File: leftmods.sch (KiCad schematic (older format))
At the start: 0 parts

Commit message: Added left modifiers to schematic
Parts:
- added DLM1, DLM2, DLM3: 1N4148WS, symbol D
- added LA1, LA2, LA3, LC2, LW1, LW2: MX-1.5U, symbol MX-1.5U
- added LC1: MX-1.25U, symbol MX-1.25U
- added RLM1, RLM2, RLM?: 2.2k, symbol R
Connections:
- new net: DLM1.1 (K), LC1.1 (COL), LC2.1 (COL)
- new net: LC1.3 (LED), LC2.3 (LED), RLM1.1
- new net: DLM2.1 (K), LA1.1 (COL), LW1.1 (COL), LW2.1 (COL)
- new net: LA1.3 (LED), LW1.3 (LED), LW2.3 (LED), RLM2.1
- new net: DLM3.1 (K), LA2.1 (COL), LA3.1 (COL)
- new net: LA2.3 (LED), LA3.3 (LED), RLM?.1
- new net leftmods5V: RLM1.2, RLM2.2, RLM?.2
- new net leftmodsLEDGND: LA1.4 (LEDGND), LA2.4 (LEDGND), LA3.4 (LEDGND), LC1.4 (LEDGND), LC2.4 (LEDGND), LW1.4 (LEDGND), LW2.4 (LEDGND)
- new net leftmodscol1: DLM1.2 (A)
- new net leftmodscol2: DLM2.2 (A)
- new net leftmodscol3: DLM3.2 (A)
- new net leftmodsrow: LA1.2 (ROW), LA2.2 (ROW), LA3.2 (ROW), LC1.2 (ROW), LC2.2 (ROW), LW1.2 (ROW), LW2.2 (ROW)

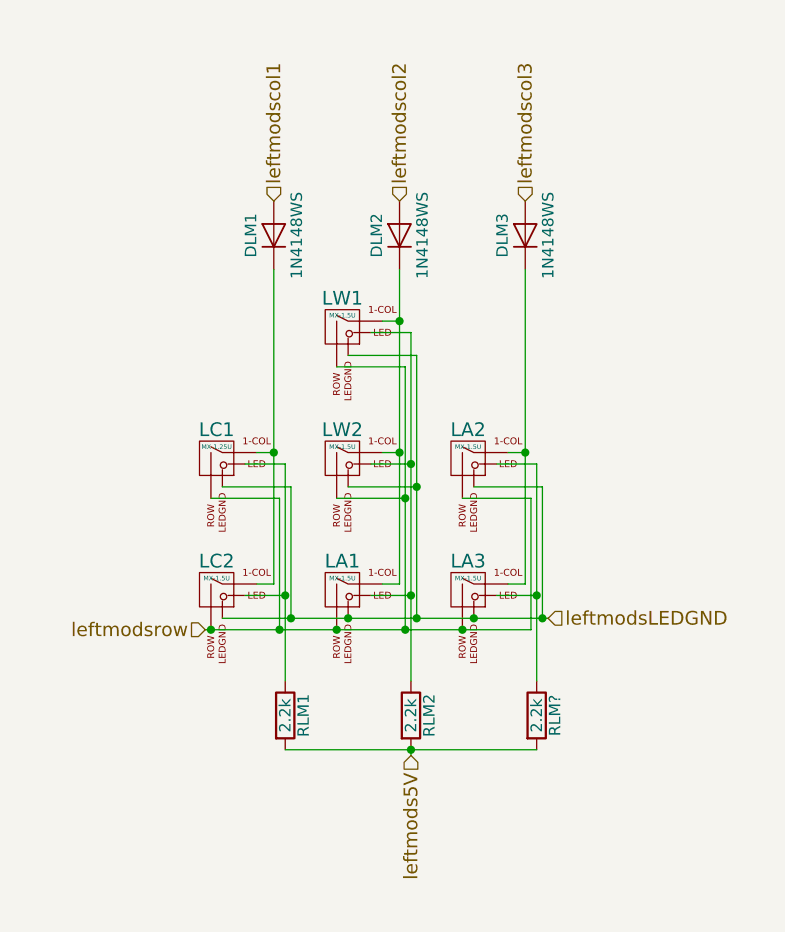
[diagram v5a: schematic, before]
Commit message: Added left mods to matrix
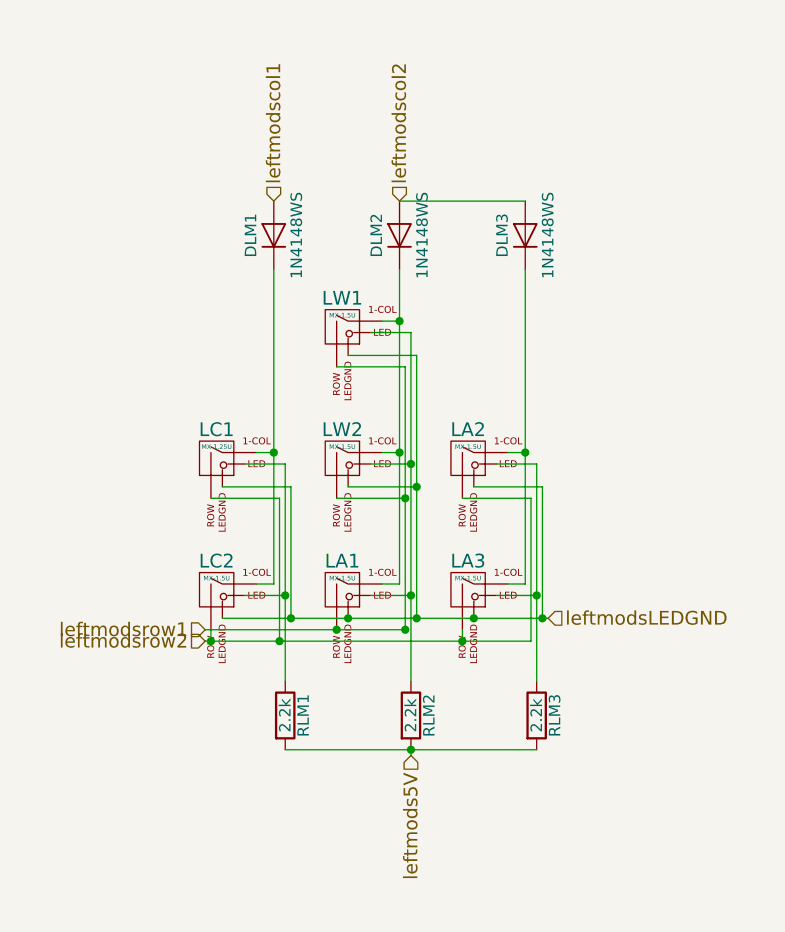
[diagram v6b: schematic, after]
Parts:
- gave numbers to parts that had none: 1
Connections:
- net leftmodscol3 is gone; now on net leftmodscol2: DLM3.2 (A)
- net leftmodsrow renamed leftmodsrow2
- net leftmodsrow2: no longer LA1.2 (ROW), LW1.2 (ROW), LW2.2 (ROW)
- new net leftmodsrow1: LA1.2 (ROW), LW1.2 (ROW), LW2.2 (ROW)
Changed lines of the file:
@@
 LIBS:valves
 LIBS:MX_Alps_Hybrids
-LIBS:Matrix-cache
+LIBS:ws2812b
+LIBS:Kairos-cache
 EELAYER 25 0
 EELAYER END
 $Descr A4 11693 8268
 encoding utf-8
-Sheet 1 6
+Sheet 6 7
 Title ""
 Date ""
@@
 $EndComp
 Text HLabel 4200 5450 0    60   Input ~ 0
-leftmodsrow
-Wire Wire Line
-	4975 4100 5050 4100
-Wire Wire Line
-	5050 3875 5050 5250
-Wire Wire Line
-	5050 4675 4975 4675
-Wire Wire Line
-	5050 5250 4975 5250
-Connection ~ 5050 4675
-Wire Wire Line
-	5525 4675 5600 4675
-Wire Wire Line
-	5600 3875 5600 5250
-Wire Wire Line
-	5600 5250 5525 5250
-Wire Wire Line
-	4425 4675 4500 4675
-Wire Wire Line
-	4500 3875 4500 5250
-Wire Wire Line
-	4500 5250 4425 5250
-Wire Wire Line
-	4775 4300 5075 4300
-Wire Wire Line
-	5075 4300 5075 5450
-Wire Wire Line
-	5075 4875 4775 4875
-Wire Wire Line
-	4200 5450 5625 5450
-Connection ~ 5075 4875
-Wire Wire Line
-	4225 4875 4525 4875
-Wire Wire Line
-	4525 4875 4525 5450
-Connection ~ 4775 5450
-Connection ~ 4525 5450
-Wire Wire Line
-	5325 4875 5625 4875
-Wire Wire Line
-	5625 4875 5625 5450
-Connection ~ 5075 5450
-Connection ~ 5325 5450
-Wire Wire Line
-	4375 4725 4550 4725
-Wire Wire Line
-	4550 4725 4550 5675
-Wire Wire Line
-	4550 5300 4375 5300
-Wire Wire Line
-	4275 5400 5700 5400
-Wire Wire Line
-	4575 5400 4575 4825
-Wire Wire Line
-	4575 4825 4275 4825
-Connection ~ 4575 5400
-Wire Wire Line
-	4925 4725 5100 4725
-Wire Wire Line
-	5100 4150 5100 5675
-Wire Wire Line
-	5100 5300 4925 5300
-Wire Wire Line
-	4925 4150 5100 4150
-Connection ~ 5100 4725
-Wire Wire Line
-	4825 4825 5125 4825
-Wire Wire Line
-	5125 4250 5125 5400
-Connection ~ 4825 5400
-Wire Wire Line
-	4825 4250 5125 4250
-Connection ~ 5125 4825
-Wire Wire Line
-	5475 4725 5650 4725
-Wire Wire Line
-	5650 4725 5650 5675
-Wire Wire Line
-	5650 5300 5475 5300
-Connection ~ 5125 5400
-Wire Wire Line
-	5675 5400 5675 4825
-Wire Wire Line
-	5675 4825 5375 4825
-Connection ~ 5375 5400
-Connection ~ 4225 5450
+leftmodsrow1
 $Comp
 L D DLM1
@@
 	0    -1   -1   0
 $EndComp
-Connection ~ 4500 4675
 $Comp
 L D DLM2
@@
 	0    -1   -1   0
 $EndComp
-Connection ~ 5050 4100
 $Comp
 L D DLM3
@@
 	0    -1   -1   0
 $EndComp
-Connection ~ 5600 4675
 Text HLabel 4500 3575 1    60   Input ~ 0
 leftmodscol1
 Text HLabel 5050 3575 1    60   Input ~ 0
 leftmodscol2
-Text HLabel 5600 3575 1    60   Input ~ 0
-leftmodscol3
 $Comp
 L R RLM1
@@
 	1    0    0    -1
 $EndComp
-Connection ~ 4550 5300
 $Comp
 L R RLM2
@@
 	1    0    0    -1
 $EndComp
-Connection ~ 5100 5300
-$Comp
-L R RLM?
+$Comp
+L R RLM3
 U 1 1 591D444F
 P 5650 5825
-F 0 "RLM?" V 5730 5825 50  0000 C CNN
+F 0 "RLM3" V 5730 5825 50  0000 C CNN
 F 1 "2.2k" V 5650 5825 50  0000 C CNN
 F 2 "" V 5580 5825 50  0000 C CNN
@@
 	1    0    0    -1
 $EndComp
+Text HLabel 5700 5400 2    60   Input ~ 0
+leftmodsLEDGND
+Text HLabel 5100 6000 3    60   Input ~ 0
+leftmods5V
+Text HLabel 4200 5500 0    60   Input ~ 0
+leftmodsrow2
+Wire Wire Line
+	4975 4100 5050 4100
+Wire Wire Line
+	5050 3875 5050 5250
+Wire Wire Line
+	5050 4675 4975 4675
+Wire Wire Line
+	5050 5250 4975 5250
+Connection ~ 5050 4675
+Wire Wire Line
+	5525 4675 5600 4675
+Wire Wire Line
+	5600 3875 5600 5250
+Wire Wire Line
+	5600 5250 5525 5250
+Wire Wire Line
+	4425 4675 4500 4675
+Wire Wire Line
+	4500 3875 4500 5250
+Wire Wire Line
+	4500 5250 4425 5250
+Wire Wire Line
+	4775 4300 5075 4300
+Wire Wire Line
+	5075 4300 5075 5450
+Wire Wire Line
+	5075 4875 4775 4875
+Wire Wire Line
+	5075 5450 4200 5450
+Connection ~ 5075 4875
+Wire Wire Line
+	4225 4875 4525 4875
+Connection ~ 4775 5450
+Wire Wire Line
+	5325 4875 5625 4875
+Wire Wire Line
+	5625 4875 5625 5500
+Connection ~ 5075 5450
+Wire Wire Line
+	4375 4725 4550 4725
+Wire Wire Line
+	4550 4725 4550 5675
+Wire Wire Line
+	4550 5300 4375 5300
+Wire Wire Line
+	4275 5400 5700 5400
+Wire Wire Line
+	4575 5400 4575 4825
+Wire Wire Line
+	4575 4825 4275 4825
+Connection ~ 4575 5400
+Wire Wire Line
+	4925 4725 5100 4725
+Wire Wire Line
+	5100 4150 5100 5675
+Wire Wire Line
+	5100 5300 4925 5300
+Wire Wire Line
+	4925 4150 5100 4150
+Connection ~ 5100 4725
+Wire Wire Line
+	4825 4825 5125 4825
+Wire Wire Line
+	5125 4250 5125 5400
+Connection ~ 4825 5400
+Wire Wire Line
+	4825 4250 5125 4250
+Connection ~ 5125 4825
+Wire Wire Line
+	5475 4725 5650 4725
+Wire Wire Line
+	5650 4725 5650 5675
+Wire Wire Line
+	5650 5300 5475 5300
+Connection ~ 5125 5400
+Wire Wire Line
+	5675 5400 5675 4825
+Wire Wire Line
+	5675 4825 5375 4825
+Connection ~ 5375 5400
+Connection ~ 4500 4675
+Connection ~ 5050 4100
+Connection ~ 5600 4675
+Connection ~ 4550 5300
+Connection ~ 5100 5300
 Connection ~ 5650 5300
 Wire Wire Line
 	4550 5975 5650 5975
 Connection ~ 5100 5975
-Text HLabel 5700 5400 2    60   Input ~ 0
-leftmodsLEDGND
 Connection ~ 5675 5400
-Text HLabel 5100 6000 3    60   Input ~ 0
-leftmods5V
 Wire Wire Line
 	5100 6000 5100 5975
+Wire Wire Line
+	5625 5500 4200 5500
+Wire Wire Line
+	4225 5500 4225 5450
+Wire Wire Line
+	4525 4875 4525 5500
+Connection ~ 4225 5500
+Wire Wire Line
+	5325 5500 5325 5450
+Connection ~ 4525 5500
+Connection ~ 5325 5500
+Wire Wire Line
+	5050 3575 5600 3575
 $EndSCHEMATC

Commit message: Fix all key annotations
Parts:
- renumbered LA1 to K_LA1, LA2 to K_LA2, LA3 to K_LA3, LC1 to K_LC1, LC2 to K_LC2, LW1 to K_LW1, LW2 to K_LW2
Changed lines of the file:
@@
 $EndDescr
 $Comp
-L MX-1.25U LC1
+L MX-1.25U K_LC1
 U 1 1 591D07B9
 P 4250 4700
-F 0 "LC1" H 4250 4825 60  0000 C CNN
+F 0 "K_LC1" H 4250 4825 60  0000 C CNN
 F 1 "MX-1.25U" H 4250 4750 20  0000 C CNN
 F 2 "" H 4225 4675 60  0001 C CNN
@@
 $EndComp
 $Comp
-L MX-1.5U LC2
+L MX-1.5U K_LC2
 U 1 1 591D088F
 P 4250 5275
-F 0 "LC2" H 4250 5400 60  0000 C CNN
+F 0 "K_LC2" H 4250 5400 60  0000 C CNN
 F 1 "MX-1.5U" H 4250 5325 20  0000 C CNN
 F 2 "" H 4225 5250 60  0001 C CNN
@@
 $EndComp
 $Comp
-L MX-1.5U LW2
+L MX-1.5U K_LW2
 U 1 1 591D08D6
 P 4800 4700
-F 0 "LW2" H 4800 4825 60  0000 C CNN
+F 0 "K_LW2" H 4800 4825 60  0000 C CNN
 F 1 "MX-1.5U" H 4800 4750 20  0000 C CNN
 F 2 "" H 4775 4675 60  0001 C CNN
@@
 $EndComp
 $Comp
-L MX-1.5U LA1
+L MX-1.5U K_LA1
 U 1 1 591D0916
 P 4800 5275
-F 0 "LA1" H 4800 5400 60  0000 C CNN
+F 0 "K_LA1" H 4800 5400 60  0000 C CNN
 F 1 "MX-1.5U" H 4800 5325 20  0000 C CNN
 F 2 "" H 4775 5250 60  0001 C CNN
@@
 $EndComp
 $Comp
-L MX-1.5U LW1
+L MX-1.5U K_LW1
 U 1 1 591D095C
 P 4800 4125
-F 0 "LW1" H 4800 4250 60  0000 C CNN
+F 0 "K_LW1" H 4800 4250 60  0000 C CNN
 F 1 "MX-1.5U" H 4800 4175 20  0000 C CNN
 F 2 "" H 4775 4100 60  0001 C CNN
@@
 $EndComp
 $Comp
-L MX-1.5U LA2
+L MX-1.5U K_LA2
 U 1 1 591D0EC8
 P 5350 4700
-F 0 "LA2" H 5350 4825 60  0000 C CNN
+F 0 "K_LA2" H 5350 4825 60  0000 C CNN
 F 1 "MX-1.5U" H 5350 4750 20  0000 C CNN
 F 2 "" H 5325 4675 60  0001 C CNN
@@
 $EndComp
 $Comp
-L MX-1.5U LA3
+L MX-1.5U K_LA3
 U 1 1 591D0F45
 P 5350 5275
-F 0 "LA3" H 5350 5400 60  0000 C CNN
+F 0 "K_LA3" H 5350 5400 60  0000 C CNN
 F 1 "MX-1.5U" H 5350 5325 20  0000 C CNN
 F 2 "" H 5325 5250 60  0001 C CNN
